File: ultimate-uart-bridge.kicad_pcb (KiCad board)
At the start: 2 copper layers, 20 parts, among them J101 USB_B_Micro, J102 Conn_01x03, J103 Conn_01x03

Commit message: First Routing
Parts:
- FB101: footprint Filter:Filter_1411-5_1.4x1.1mm -> Ferrite_THT:LairdTech_28C0236-0JW-10
- moved R102 25.7 mm to (113.0, 90.2)
- moved C104 25.2 mm to (113.0, 87.6)
- moved R101 24.3 mm to (113.0, 94.0)
- moved C106 21.9 mm to (118.1, 96.5), turned to 180 degrees
- moved C108 21.9 mm to (118.1, 99.1), turned to 180 degrees
- moved J102 21.7 mm to (132.1, 86.4), turned to 0 degrees
- moved D101 15.6 mm to (135.9, 84.8), turned to 90 degrees
- moved I101 13.1 mm to (123.2, 83.8)
- moved J103 10.5 mm to (143.5, 92.7)
- moved R104 9.92 mm to (139.7, 90.2), turned to 270 degrees
- moved C102 9.84 mm to (128.3, 84.1), turned to 90 degrees
- moved R103 8.76 mm to (135.9, 89.9), turned to 270 degrees
- moved D102 8.62 mm to (139.7, 84.8), turned to 90 degrees
- moved I102 6.48 mm to (124.5, 92.7), turned to 180 degrees
- moved C103 5.68 mm to (113.0, 96.5), turned to 0 degrees
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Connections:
- net USB_DM renamed USBD_N
- net USB_DP renamed USBD_P
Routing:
- net VBUS: track 0.00 -> 46.0 mm, vias 0 -> 2
- net /PCTX: track 0.00 -> 34.1 mm, vias 0 -> 1
- net GND: track 0.00 -> 33.6 mm, vias 0 -> 32
- net /RXLED#: track 0.00 -> 26.6 mm, vias 0 -> 2
- net VCCIO: track 0.00 -> 24.7 mm
- net /PCRX: track 0.00 -> 19.8 mm, vias 0 -> 3
- net /TXLED#: track 0.00 -> 18.4 mm, vias 0 -> 2
- net USBD_N: track 0.00 -> 17.0 mm, vias 0 -> 4
- net USBD_P: track 0.00 -> 15.1 mm, vias 0 -> 2
- net Net-(FB101-Pad2): track 0.00 -> 14.2 mm
- net +3V3: track 0.00 -> 13.1 mm, vias 0 -> 1
- net Net-(C104-Pad1): track 0.00 -> 8.58 mm
- net +1V8: track 0.00 -> 8.51 mm
- net Net-(C103-Pad1): track 0.00 -> 8.37 mm
- net Net-(D102-Pad1): track 0.00 -> 3.30 mm
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- added copper zone on B.Cu, net GND
- added copper zone on F.Cu, net GND
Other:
- board outline added: 45.7 x 29.2 mm
- net class Default: trace_width 0.25 -> 0.2; via_dia 0.8 -> 0.7
- rule trace_min: 0.2 -> 0.128
- rule via_min_size: 0.4 -> 0.6
- board text added: "GND"
- board text added: "JLCJLCJLCJLC"
- board text added: "PCRX"
- board text added: "PCTX"
- board text added: "RX"
- board text added: "TX"
- board text added: "Ultimate UART Bridge Thomas Fike Rev 1 12/20/21"

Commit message: New inital routing
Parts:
- added R105: 5.1k, Resistor_SMD:R_0805_2012Metric_Pad1.20x1.40mm_HandSolder, F.Cu at (101.9, 71.4)
- added R106: 5.1k, Resistor_SMD:R_0805_2012Metric_Pad1.20x1.40mm_HandSolder, F.Cu at (105.2, 71.4)
- added kibuzzard-62CBA051: G***, kibuzzard-62CBA051, F.Cu at (159.5, 74.2)
- added kibuzzard-62CBA0C9: G***, kibuzzard-62CBA0C9, F.Cu at (159.5, 88.1)
- added kibuzzard-62CBA130: G***, kibuzzard-62CBA130, F.Cu at (162.1, 80.8)
- added kibuzzard-62CBA316: G***, kibuzzard-62CBA316, F.Cu at (149.4, 79.0)
- added kibuzzard-62CBA331: G***, kibuzzard-62CBA331, F.Cu at (145.3, 79.0)
- added kibuzzard-62CBA409: G***, kibuzzard-62CBA409, F.Cu at (140.2, 81.8)
- added kibuzzard-62CBA40F: G***, kibuzzard-62CBA40F, F.Cu at (137.2, 81.8)
- added kibuzzard-62CBA429: G***, kibuzzard-62CBA429, F.Cu at (134.1, 81.8)
- added kibuzzard-62CBA9F2: G***, kibuzzard-62CBA9F2, F.Cu at (132.6, 91.4)
- FB101: footprint Ferrite_THT:LairdTech_28C0236-0JW-10 -> Inductor_SMD:L_0805_2012Metric_Pad1.15x1.40mm_HandSolder
- I101: footprint footprints:MIC5317-1.8YM5-TR -> Package_TO_SOT_SMD:SOT-23-5_HandSoldering
- J101: value USB_B_Micro -> Conn_02x03_Row_Letter_First; footprint Connector_USB:USB_Micro-B_Molex_47346-0001 -> Connector_PinHeader_2.54mm:PinHeader_2x03_P2.54mm_Vertical_SMD
- J102: value Conn_01x03 -> USB_C_Receptacle_USB2.0; footprint Connector_PinHeader_2.54mm:PinHeader_1x03_P2.54mm_Vertical -> Connector_USB:USB_C_Receptacle_GCT_USB4085
- J103: footprint Connector_PinHeader_2.54mm:PinHeader_1x03_P2.54mm_Horizontal -> Connector_PinHeader_2.54mm:PinHeader_1x03_P2.54mm_Vertical_SMD_Pin1Left
- moved J101 37.2 mm to (137.2, 73.4), turned to 90 degrees
- moved J102 27.7 mm to (105.6, 78.3), turned to -90 degrees
- moved C105 20.3 mm to (123.7, 76.7), turned to 180 degrees
- moved J103 17.6 mm to (156.5, 80.8), turned to 180 degrees
- moved C106 17.6 mm to (101.6, 90.4), turned to -90 degrees
- moved C107 14.8 mm to (105.2, 90.4), turned to -90 degrees
- moved R101 14.5 mm to (112.0, 79.5)
- moved D101 14.1 mm to (149.4, 80.8)
- moved R103 13.7 mm to (149.4, 87.4)
- moved C108 13.0 mm to (108.5, 90.4), turned to -90 degrees
- moved C102 11.8 mm to (123.7, 73.2), turned to 0 degrees
- moved C101 10.7 mm to (112.0, 72.1), turned to 180 degrees
- moved I102 9.68 mm to (123.7, 83.1)
- moved I101 9.66 mm to (117.6, 75.9)
- moved R102 8.70 mm to (112.0, 81.5)
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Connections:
- D101 pad 2: VCCIO -> +3V3
- D102 pad 2: VCCIO -> +3V3
- I101 pad 4: Net-(I101-Pad4) -> unconnected-(I101-Pad4)
- I102 pad 1: Net-(I102-Pad1) -> unconnected-(I102-Pad1)
- I102 pad 18: Net-(I102-Pad18) -> unconnected-(I102-Pad18)
- I102 pad 19: Net-(I102-Pad19) -> unconnected-(I102-Pad19)
- I102 pad 2: Net-(I102-Pad2) -> unconnected-(I102-Pad2)
- I102 pad 5: Net-(I102-Pad5) -> unconnected-(I102-Pad5)
- I102 pad 7: Net-(I102-Pad7) -> unconnected-(I102-Pad7)
- I102 pad 8: Net-(I102-Pad8) -> unconnected-(I102-Pad8)
- I102 pad 9: Net-(I102-Pad9) -> unconnected-(I102-Pad9)
- J101 pad 1: Net-(FB101-Pad2) -> VCCIO
- J101 pad 2: Net-(C104-Pad1) -> VBUS
- J101 pad 3: Net-(C103-Pad1) -> VCCIO
- J101 pad 4: Net-(J101-Pad4) -> +3V3
- J101 pad 5: GND -> VCCIO
- J101 pad 6: GND -> +1V8
- R101 pad 1: Net-(C103-Pad1) -> Net-(C104-Pad1)
- R102 pad 1: Net-(C104-Pad1) -> Net-(C103-Pad1)
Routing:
- net GND: track 33.6 -> 0.00 mm, vias 32 -> 0
- net +3V3: track 13.1 -> 40.2 mm, vias 1 -> 0
- net VBUS: track 46.0 -> 73.0 mm, vias 2 -> 5
- net +1V8: track 8.51 -> 26.1 mm
- net /PCRX: track 19.8 -> 36.1 mm, vias 3 -> 2
- net Net-(J102-PadB5): track 0.00 -> 11.9 mm, vias 0 -> 2
- net Net-(J102-PadA5): track 0.00 -> 10.7 mm, vias 0 -> 1
- net /TXLED#: track 18.4 -> 28.3 mm
- net VCCIO: track 24.7 -> 33.8 mm
- net Net-(C104-Pad1): track 8.58 -> 17.5 mm, vias 0 -> 2
- net USBD_N: track 17.0 -> 8.45 mm, vias 4 -> 0
- net Net-(C103-Pad1): track 8.37 -> 16.9 mm
- net /PCTX: track 34.1 -> 42.5 mm, vias 1 -> 0
- net /RXLED#: track 26.6 -> 34.1 mm
- net USBD_P: track 15.1 -> 8.45 mm, vias 2 -> 0
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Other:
- board size 45.7 x 29.2 mm -> 67.1 x 26.4 mm
- net class Default removed
- board text removed: "GND"
- board text removed: "JLCJLCJLCJLC"
- board text removed: "PCRX"
- board text removed: "PCTX"
- board text removed: "RX"
- board text removed: "TX"
- board text removed: "Ultimate UART Bridge Thomas Fike Rev 1 12/20/21"

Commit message: GND stiching
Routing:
- net GND: track 0.00 -> 3.78 mm, vias 0 -> 30
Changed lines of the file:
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@@
   )
   (gr_rect (start 99.568 93.98) (end 166.624 67.564) (layer "Edge.Cuts") (width 0.05) (fill none))
+  (segment (start 117.602 75.204498) (end 117.602 74.596) (width 0.2) (layer "F.Cu") (net 1))
+  (segment (start 125.362252 82.7405) (end 126.298 82.7405) (width 0.2) (layer "F.Cu") (net 1))
+  (segment (start 116.84 75.966498) (end 117.602 75.204498) (width 0.2) (layer "F.Cu") (net 1))
+  (segment (start 122.247502 83.361) (end 121.1125 83.361) (width 0.2) (layer "F.Cu") (net 1))
+  (segment (start 121.1125 83.361) (end 121.098 83.3755) (width 0.2) (layer "F.Cu") (net 1))
+  (via (at 129.54 77.724) (size 0.7) (drill 0.4) (layers "F.Cu" "B.Cu") (free) (net 1))
+  (via (at 115.824 84.328) (size 0.7) (drill 0.4) (layers "F.Cu" "B.Cu") (free) (net 1))
+  (via (at 122.247502 83.361) (size 0.7) (drill 0.4) (layers "F.Cu" "B.Cu") (free) (net 1))
+  (via (at 100.584 83.82) (size 0.7) (drill 0.4) (layers "F.Cu" "B.Cu") (free) (net 1))
+  (via (at 102.616 84.328) (size 0.7) (drill 0.4) (layers "F.Cu" "B.Cu") (free) (net 1))
+  (via (at 125.362252 82.7405) (size 0.7) (drill 0.4) (layers "F.Cu" "B.Cu") (free) (net 1))
+  (via (at 164.084 78.74) (size 0.7) (drill 0.4) (layers "F.Cu" "B.Cu") (free) (net 1))
+  (via (at 116.84 69.088) (size 0.7) (drill 0.4) (layers "F.Cu" "B.Cu") (free) (net 1))
+  (via (at 100.584 78.74) (size 0.7) (drill 0.4) (layers "F.Cu" "B.Cu") (free) (net 1))
+  (via (at 164.084 91.44) (size 0.7) (drill 0.4) (layers "F.Cu" "B.Cu") (free) (net 1))
+  (via (at 152.908 91.44) (size 0.7) (drill 0.4) (layers "F.Cu" "B.Cu") (free) (net 1))
+  (via (at 127.508 75.692) (size 0.7) (drill 0.4) (layers "F.Cu" "B.Cu") (free) (net 1))
+  (via (at 164.084 71.12) (size 0.7) (drill 0.4) (layers "F.Cu" "B.Cu") (free) (net 1))
+  (via (at 108.712 69.088) (size 0.7) (drill 0.4) (layers "F.Cu" "B.Cu") (free) (net 1))
+  (via (at 141.224 88.392) (size 0.7) (drill 0.4) (layers "F.Cu" "B.Cu") (free) (net 1))
+  (via (at 108.204 84.328) (size 0.7) (drill 0.4) (layers "F.Cu" "B.Cu") (free) (net 1))
+  (via (at 159.512 69.088) (size 0.7) (drill 0.4) (layers "F.Cu" "B.Cu") (free) (net 1))
+  (via (at 130.048 83.82) (size 0.7) (drill 0.4) (layers "F.Cu" "B.Cu") (free) (net 1))
+  (via (at 148.336 70.612) (size 0.7) (drill 0.4) (layers "F.Cu" "B.Cu") (free) (net 1))
+  (via (at 104.14 75.692) (size 0.7) (drill 0.4) (layers "F.Cu" "B.Cu") (free) (net 1))
+  (via (at 103.632 87.884) (size 0.7) (drill 0.4) (layers "F.Cu" "B.Cu") (free) (net 1))
+  (via (at 108.204 86.868) (size 0.7) (drill 0.4) (layers "F.Cu" "B.Cu") (free) (net 1))
+  (via (at 164.084 74.676) (size 0.7) (drill 0.4) (layers "F.Cu" "B.Cu") (free) (net 1))
+  (via (at 129.54 70.612) (size 0.7) (drill 0.4) (layers "F.Cu" "B.Cu") (free) (net 1))
+  (via (at 116.84 75.966498) (size 0.7) (drill 0.4) (layers "F.Cu" "B.Cu") (free) (net 1))
+  (via (at 164.084 84.328) (size 0.7) (drill 0.4) (layers "F.Cu" "B.Cu") (free) (net 1))
+  (via (at 114.808 77.216) (size 0.7) (drill 0.4) (layers "F.Cu" "B.Cu") (free) (net 1))
+  (via (at 106.68 92.964) (size 0.7) (drill 0.4) (layers "F.Cu" "B.Cu") (free) (net 1))
+  (via (at 132.588 88.392) (size 0.7) (drill 0.4) (layers "F.Cu" "B.Cu") (free) (net 1))
+  (via (at 129.54 88.392) (size 0.7) (drill 0.4) (layers "F.Cu" "B.Cu") (free) (net 1))
   (segment (start 113.039 75.946) (end 113.039 72.1485) (width 0.3) (layer "F.Cu") (net 2))
   (segment (start 119.9515 82.7405) (end 119.888 82.804) (width 0.3) (layer "F.Cu") (net 2))

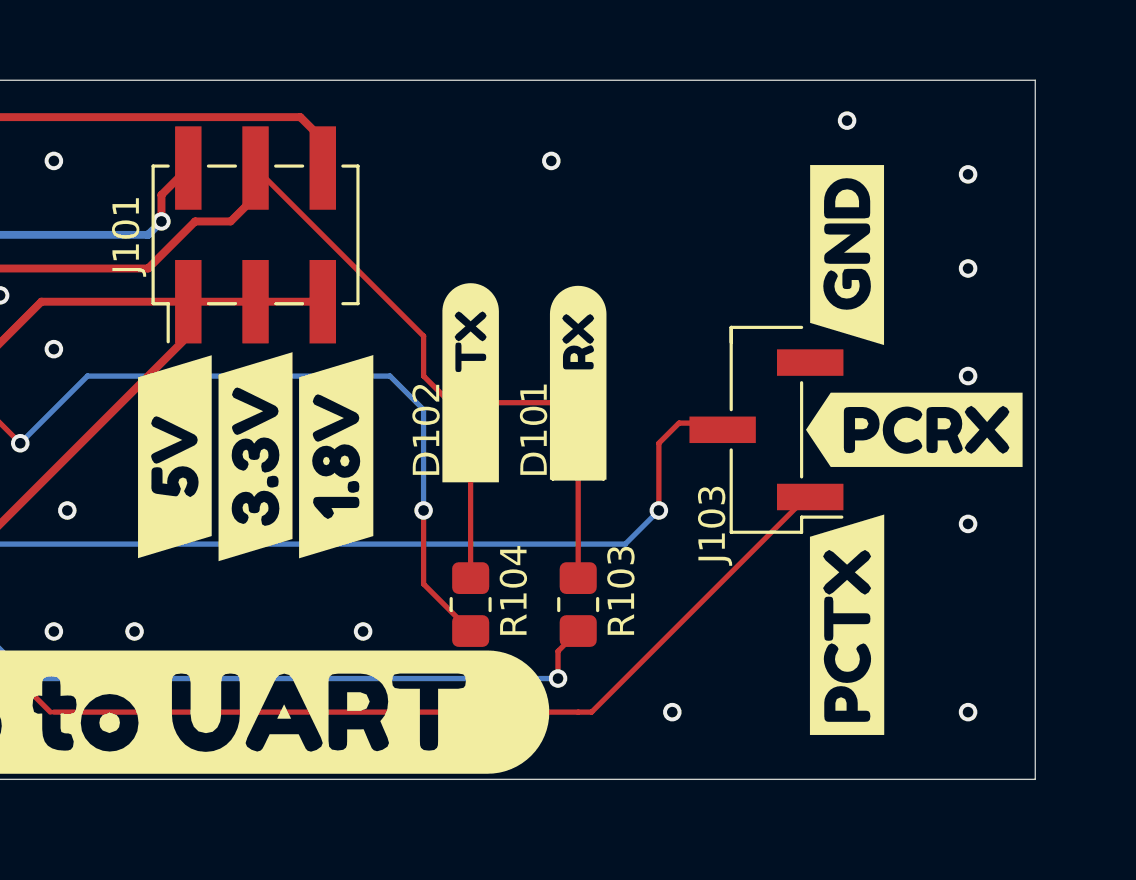
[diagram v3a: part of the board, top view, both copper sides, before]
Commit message: Add testpoints and text
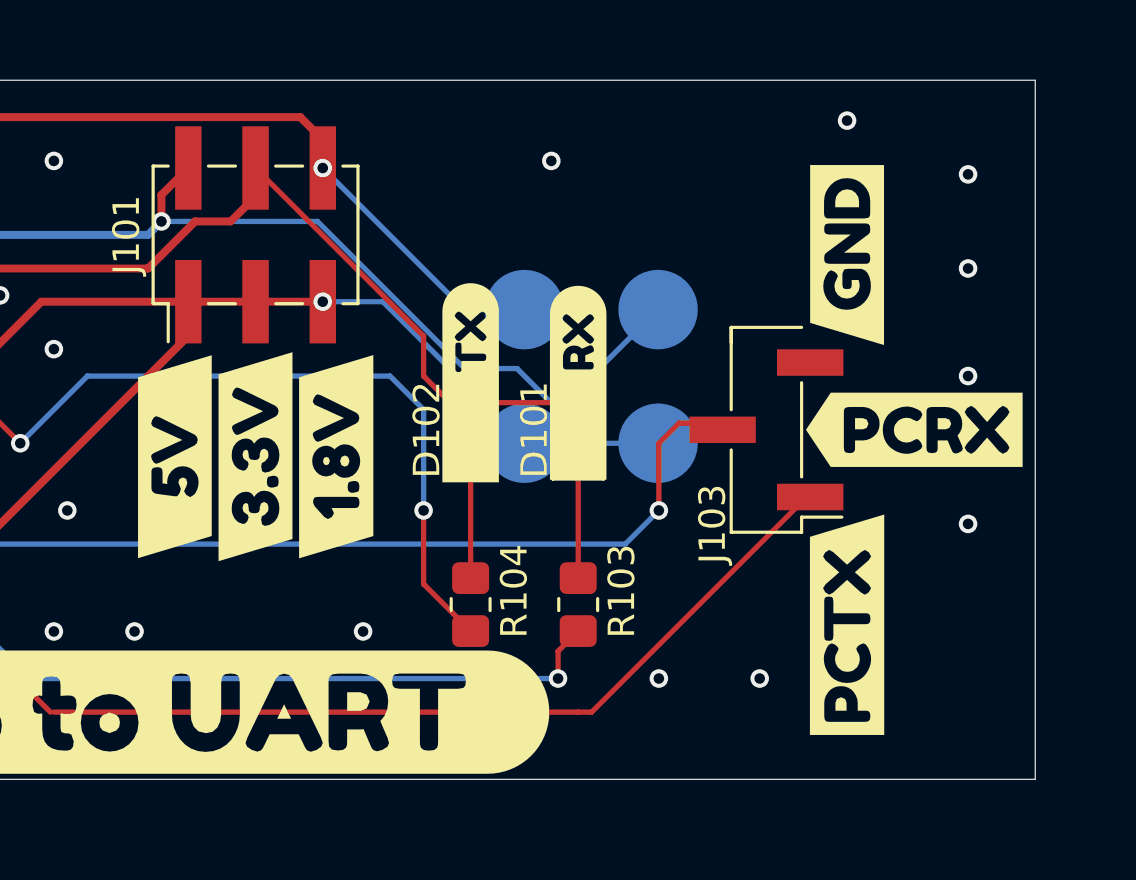
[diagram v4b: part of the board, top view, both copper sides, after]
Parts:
- added +1V8: TestPoint, TestPoint:TestPoint_Pad_D3.0mm, B.Cu at (147.3, 76.2)
- added +3V3: TestPoint, TestPoint:TestPoint_Pad_D3.0mm, B.Cu at (152.4, 76.2)
- added VBUS: TestPoint, TestPoint:TestPoint_Pad_D3.0mm, B.Cu at (152.4, 81.3)
- added VCCIO: TestPoint, TestPoint:TestPoint_Pad_D3.0mm, B.Cu at (147.3, 81.3)
- added kibuzzard-62D45EE7: G***, kibuzzard-62D45EE7, B.Cu at (104.1, 69.8)
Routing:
- net VBUS: track 73.0 -> 95.2 mm
- net VCCIO: track 33.8 -> 43.7 mm, vias 0 -> 1
- net +1V8: track 26.1 -> 35.9 mm, vias 0 -> 1
- net +3V3: track 40.2 -> 45.0 mm, vias 0 -> 1
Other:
- board text added: "JLCJLCJLCJLC"
- board text added: "Ultimate UART Bridge V1 July 2022 Thomas Fike https://github.com/ThomasFike/ultimate-uart-bridge"

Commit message: Update Production Files
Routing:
- net GND: track 3.78 -> 6.48 mm
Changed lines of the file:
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@@
   (segment (start 117.602 75.204498) (end 117.602 74.596) (width 0.2) (layer "F.Cu") (net 1))
   (segment (start 125.362252 82.7405) (end 126.298 82.7405) (width 0.2) (layer "F.Cu") (net 1))
+  (segment (start 104.275 84.255) (end 105.625 84.255) (width 0.2) (layer "F.Cu") (net 1))
   (segment (start 116.84 75.966498) (end 117.602 75.204498) (width 0.2) (layer "F.Cu") (net 1))
+  (segment (start 104.275 78.305) (end 105.625 78.305) (width 0.2) (layer "F.Cu") (net 1))
   (segment (start 122.247502 83.361) (end 121.1125 83.361) (width 0.2) (layer "F.Cu") (net 1))
   (segment (start 121.1125 83.361) (end 121.098 83.3755) (width 0.2) (layer "F.Cu") (net 1))
